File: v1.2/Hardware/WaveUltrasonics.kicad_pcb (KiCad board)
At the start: 2 copper layers, 257 x 128 mm, 220 parts, among them J1 MAINS_IN, J10 DG25C-B-04P-13-00AH, J2 L-KLS1-207-2-08-S, J3 Screw_Terminal_01x03, J4 DS1069-02MVW6X, J5 Conn_01x04, J6 DS1069-04MVW6X, J7 DS1069-02MVW6X, J8 DS1069-04MVW6X, J9 DG25C-B-04P-13-00AH, Q1 IXGH48N60C3D1, Q10 BC556, Q15 MMBT3904, Q16 MMBT3904, Q17 MMBT3904, Q18 MMBT3904, Q19 MMBT3904, Q2 IXGH48N60C3D1, Q20 MMBT3904, Q21 BC817, Q22 BC817, Q23 BC817, Q24 BC817, Q5 BC546, Q6 BC556, Q7 BC546, Q8 BC556, Q9 BC546, T2 Transformer_1P_2S, T3 Transformer_1P_2S, U1 4N39, U10 ACPL-7900, U12 OPA228, U13 L78L05_SOT89, U14 TLV1117-33, U15 4N25, U16 ADM2483xRW, U17 STM32F334C8Tx, U2 4N39, U3 MCP6022, U4 ACPL-7900, U5 TL431LP, U6 L7805, U7 TLV73333PDBV, U8 HCPL-3120, U9 HCPL-3120, Y1 8MHz

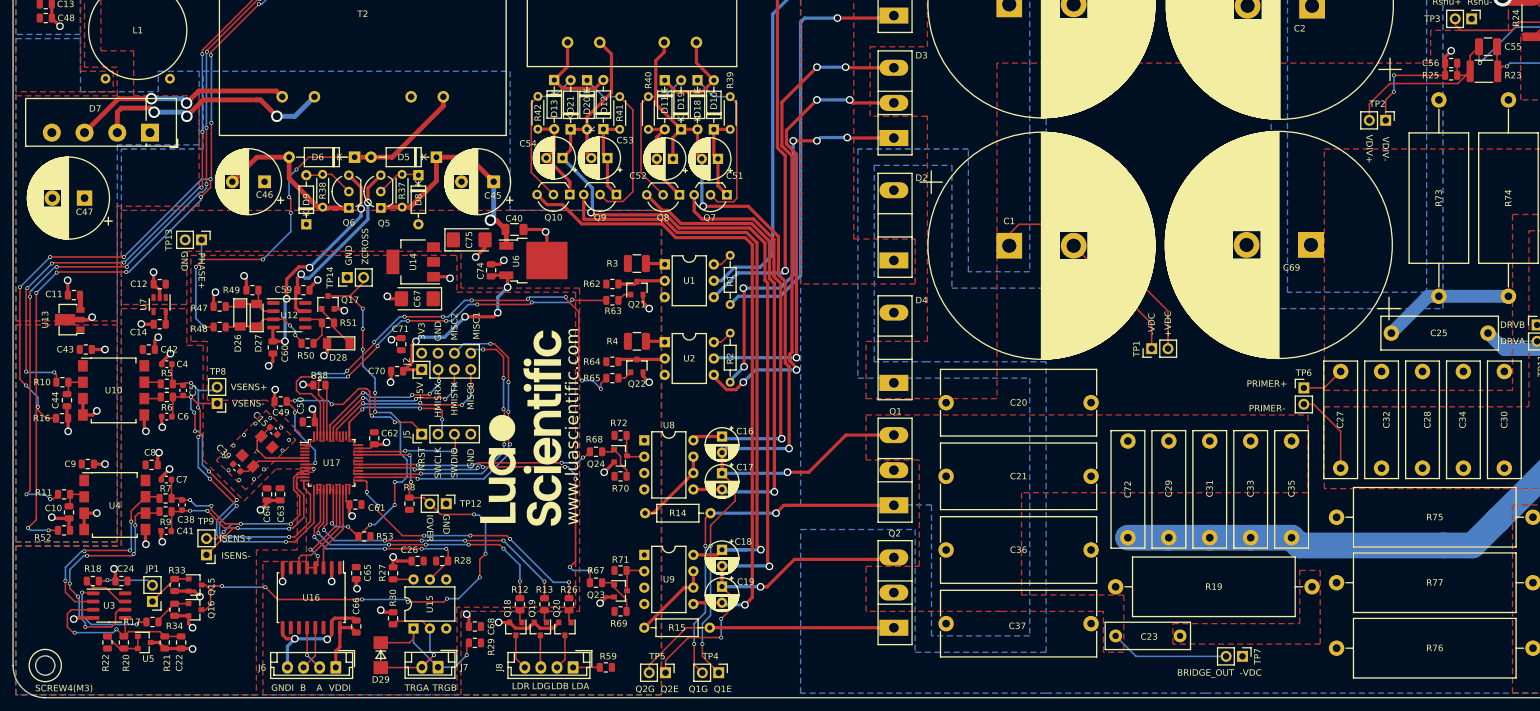
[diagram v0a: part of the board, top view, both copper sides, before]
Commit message: Addition of firmware to v1.2(not tested)
+Addition of power tracking(with duty cycle control).
+Addition of resonance freq tracking(via proprietary algorithm relied on active and reactive power measurements)
+Quality factor monitoring
+Power boost when loaded(idle and loaded modes)
+Much better frequency resolution(less than 1Hz)
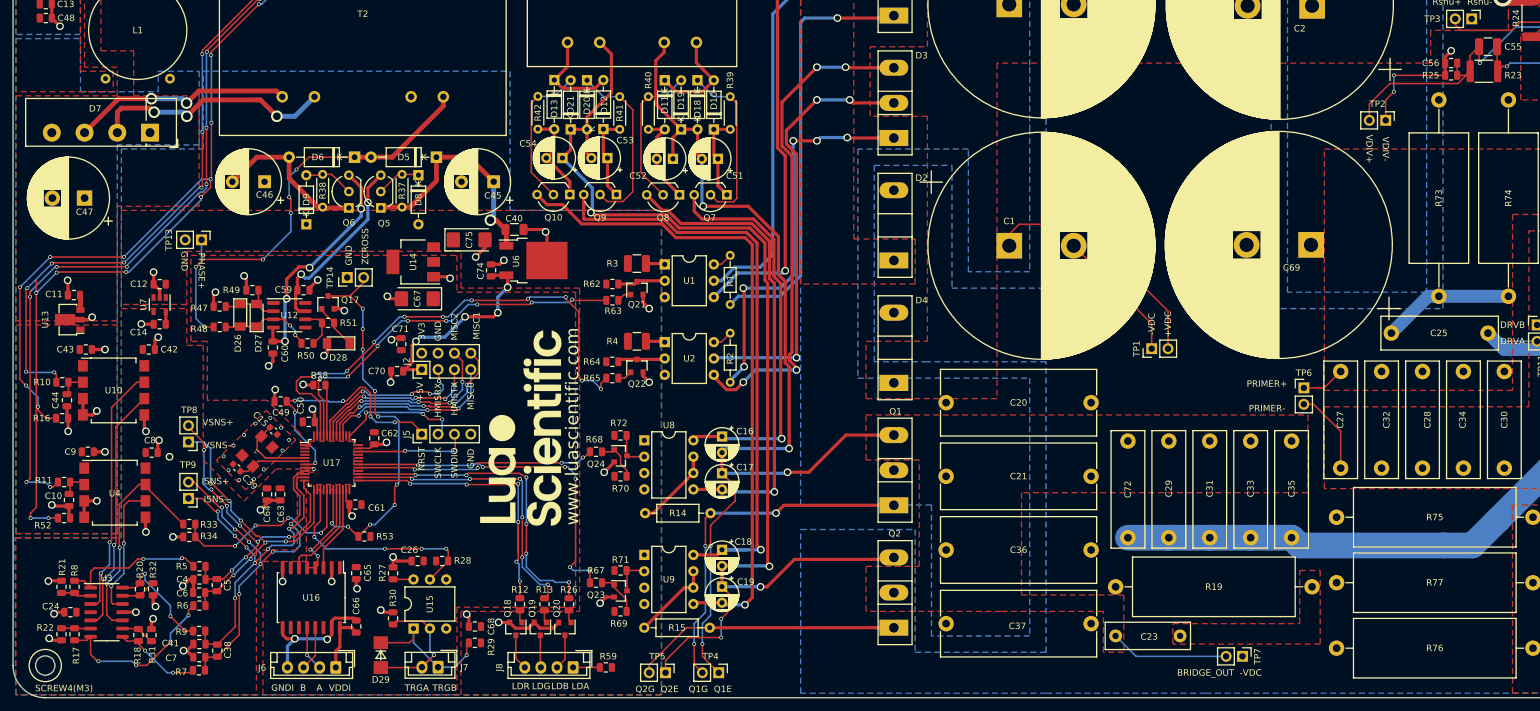
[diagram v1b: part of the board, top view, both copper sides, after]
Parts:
- removed C22: 2.2u, Capacitor_SMD:C_0805_2012Metric
- removed JP1: Jumper_NO_Small, Connector_PinHeader_2.54mm:PinHeader_1x02_P2.54mm_Vertical
- removed Q15, Q16: MMBT3904, Package_TO_SOT_SMD:SOT-23
- removed TP12: TestPoint_2Pole, Connector_PinHeader_2.54mm:PinHeader_1x02_P2.54mm_Vertical
- removed U5: TL431LP, Package_TO_SOT_SMD:SOT-23
- added R31: 3.3k %0.1, Resistor_SMD:R_0805_2012Metric, F.Cu at (88.0, 176.3)
- added R32: 3.3k %0.1, Resistor_SMD:R_0805_2012Metric, F.Cu at (88.2, 169.2)
- C38, C4, C41, C5, C6, C7: footprint Capacitor_SMD:C_0603_1608Metric -> Capacitor_SMD:C_0805_2012Metric
- R17, R18: value 2.2k -> 1k %0.1
- R20: value 20k %0.1 -> 1k %0.1
- R21: value 22k %0.1 -> 3.3k %0.1
- R22: value 2.2k -> 3.3k %0.1
- R33, R34: value 1k -> 1k %1
- R8: value 120R -> 1k %0.1
- U3: value MCP6022 -> MCP6024; footprint Package_SO:SOIC-8_3.9x4.9mm_P1.27mm -> Package_SO:SOIC-14_3.9x8.7mm_P1.27mm
- moved R8 53.5 mm to (76.0, 168.8)
- moved C4 33.8 mm to (95.4, 167.6)
- moved R6 32.8 mm to (95.4, 171.7)
- moved C5 30.7 mm to (98.1, 168.5)
- moved R5 28.8 mm to (95.4, 165.6)
- moved C7 28.0 mm to (95.4, 179.7)
- moved C6 27.8 mm to (95.4, 169.7)
- moved R7 27.2 mm to (95.4, 181.7)
- moved C38 23.3 mm to (98.2, 178.7), turned to 90 degrees
- moved R9 19.3 mm to (95.4, 175.6)
- moved C41 18.3 mm to (95.4, 177.7)
- moved R21 18.2 mm to (74.0, 168.8)
- moved R17 12.2 mm to (76.0, 176.1), turned to 90 degrees
- moved R34 11.5 mm to (93.9, 161.0), turned to 0 degrees
- moved R18 11.0 mm to (85.9, 176.3), turned to 90 degrees
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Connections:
- R17 pad 1: Net-(Q16-Pad1) -> Net-(R17-Pad1)
- R18 pad 1: Net-(JP1-Pad2) -> Net-(R18-Pad1)
- R20 pad 2: Net-(C22-Pad1) -> Net-(R20-Pad2)
- R21 pad 1: GND -> Net-(R21-Pad1)
- R21 pad 2: Net-(C22-Pad1) -> GND
- R22 pad 1: Net-(R20-Pad1) -> Net-(R17-Pad2)
- R22 pad 2: VDDA -> GND
- R33 pad 1: GND -> /CURRENT_PRO_SENS
- R33 pad 2: Net-(JP1-Pad1) -> Net-(R33-Pad2)
- R34 pad 2: Net-(Q16-Pad1) -> /CURRENT_PRO_SENS
- R6 pad 2: Net-(R6-Pad2) -> Net-(R17-Pad1)
- R7 pad 2: Net-(R7-Pad2) -> Net-(R18-Pad1)
- R8 pad 1: /OVERCURRENT -> Net-(R5-Pad2)
- R8 pad 2: VDD -> Net-(R21-Pad1)
- R9 pad 2: Net-(R9-Pad2) -> Net-(R20-Pad1)
- U10 pad 6: Net-(R6-Pad2) -> Net-(U10-Pad6)
- U10 pad 7: Net-(R5-Pad2) -> Net-(U10-Pad7)
- U17 pad 16: /LED_RED -> (no net)
- U17 pad 17: /LED_GREEN -> /CURRENT_PRO_SENS
- U17 pad 25: /LED_BLUE -> /LED_RED
- U17 pad 26: /Mcu/MISC2 -> /LED_GREEN
- U17 pad 27: /Mcu/MISC1 -> /LED_BLUE
- U17 pad 33: /OVERCURRENT -> (no net)
- U17 pad 39: (no net) -> /Mcu/MISC0
- U17 pad 40: (no net) -> /Mcu/MISC1
- U17 pad 41: /Mcu/MISC0 -> /Mcu/MISC2
- U3 pad 1: Net-(R17-Pad2) -> Net-(R5-Pad2)
- U3 pad 2: Net-(R7-Pad2) -> Net-(R21-Pad1)
- U3 pad 3: Net-(C22-Pad1) -> Net-(U10-Pad7)
- U3 pad 4: GND -> VDDA
- U3 pad 5: Net-(C22-Pad1) -> Net-(U10-Pad6)
- U3 pad 6: Net-(R9-Pad2) -> Net-(R17-Pad2)
- U3 pad 7: Net-(R18-Pad2) -> Net-(R17-Pad1)
- U3 pad 8: VDDA -> Net-(R18-Pad1)
- U4 pad 6: Net-(R9-Pad2) -> Net-(U3-Pad12)
- U4 pad 7: Net-(R7-Pad2) -> Net-(R33-Pad2)
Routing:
- net /OVERCURRENT: track 87.5 -> 0.00 mm, vias 10 -> 0
- net Net-(U10-Pad7): track 0.00 -> 39.2 mm, vias 0 -> 2
- net Net-(R9-Pad2): track 39.0 -> 0.00 mm, vias 6 -> 0
- net Net-(U10-Pad6): track 0.00 -> 38.4 mm, vias 0 -> 2
- net Net-(R33-Pad2): track 0.00 -> 35.7 mm, vias 0 -> 2
- net /CURRENT_PRO_SENS: track 0.00 -> 32.0 mm, vias 0 -> 4
- net Net-(R7-Pad2): track 31.5 -> 0.00 mm, vias 4 -> 0
- net Net-(C22-Pad1): track 28.6 -> 0.00 mm, vias 2 -> 0
- net Net-(R17-Pad1): track 0.00 -> 27.2 mm, vias 0 -> 4
- net Net-(U3-Pad12): track 0.00 -> 21.3 mm, vias 0 -> 2
- net /ISENS+: track 40.0 -> 60.9 mm, vias 5 -> 7
- net Net-(R5-Pad2): track 2.66 -> 22.7 mm, vias 0 -> 2
- net /Mcu/MISC2: track 50.0 -> 30.4 mm, vias 5 -> 4
- net /ISENS-: track 40.0 -> 55.6 mm, vias 4 -> 7
- net Net-(R18-Pad1): track 0.00 -> 14.5 mm, vias 0 -> 2
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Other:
- board text added: "ISNS+"
- board text added: "ISNS-"
- board text added: "VSNS+"
- board text added: "VSNS-"
- board text removed: "IOVER"
- board text removed: "ISENS+"
- board text removed: "ISENS-"
- board text removed: "VSENS+"
- board text removed: "VSENS-"
